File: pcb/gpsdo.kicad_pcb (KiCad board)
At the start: 2 copper layers, 120 x 100 mm, 151 parts, among them IC1 ICE40LP384-SG32, J1 JTAG, J10 CLK0, J11 CLK7, J12 USB_B_Micro, J13 CLK6, J14 CLK5, J15 CLK4, J2 SSD1306, J3 EXT_CLOCK, J4 GPS_ANT, J5 USB_B_Micro, J6 CLK3, J7 Screw_Terminal_01x03, J8 CLK2, J9 CLK1, M1 E73-2G4M08S1C-52840, Q1 S9018, SW1 EC11, SW2 MCML4-112B, U1 MCP9808_MSOP, U2 MCP9808_MSOP, U3 TPS652510, U4 LT1763xS8, U5 74LVC1G17, U6 Si5351C-B-GM, U7 74LVC1G17, U8 uBlox NEO-7M, U9 AD5761R, Y1 32768, Y2 8663-XS

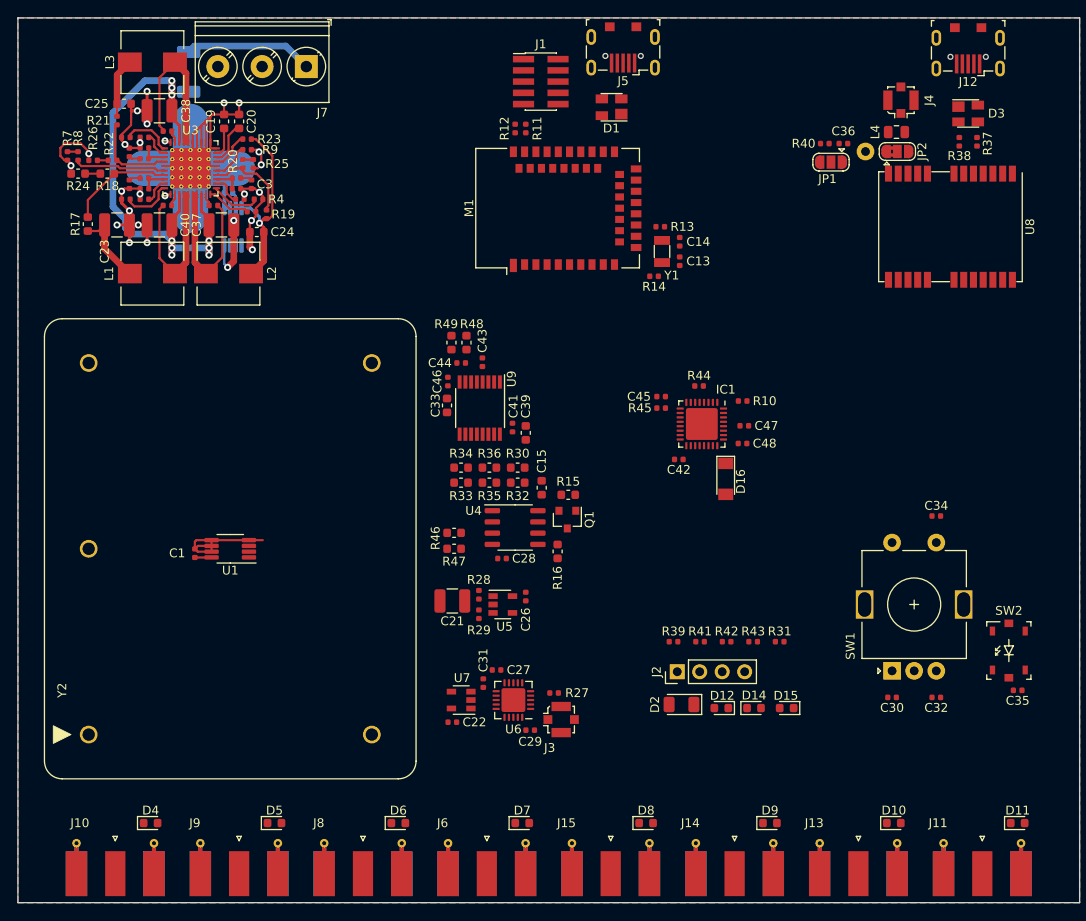
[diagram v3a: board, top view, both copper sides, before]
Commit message: pin assignment optimization, routing
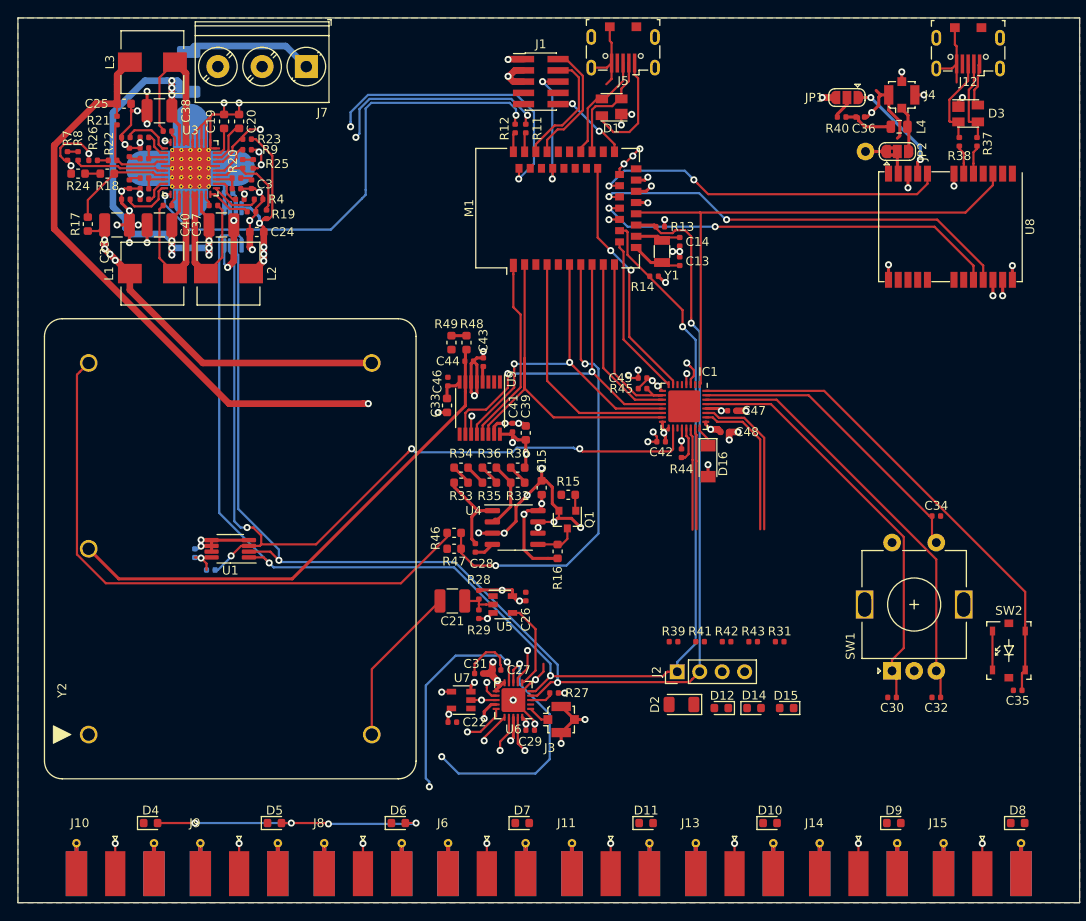
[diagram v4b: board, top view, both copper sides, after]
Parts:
- C1, R10: moved to B.Cu
- moved R10 63.1 mm to (71.8, 122.4), turned to 0 degrees
- moved D11 42.0 mm to (121.0, 151.0)
- moved D8 42.0 mm to (163.0, 151.0)
- moved J11 42.0 mm to (117.0, 155.0)
- moved J15 42.0 mm to (159.0, 155.0)
- moved D9 14.0 mm to (149.0, 151.0)
- moved J13 14.0 mm to (131.0, 155.0)
- moved J14 14.0 mm to (145.0, 155.0)
- moved D10 14.0 mm to (135.0, 151.0)
- moved R44 7.85 mm to (125.0, 109.2), turned to 270 degrees
- moved JP1 7.52 mm to (143.7, 69.0)
- moved R40 3.55 mm to (143.1, 71.2)
- moved C36 3.55 mm to (145.2, 71.2)
- moved C28 3.25 mm to (101.7, 119.9), turned to 90 degrees
- moved R45 3.04 mm to (120.6, 101.9)
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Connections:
- IC1 pad 1: (no net) -> /GPS_PULSE
- IC1 pad 18: /FPGA_INT -> /TEMP_ALERT
- IC1 pad 19: /GPS_PULSE -> (no net)
- IC1 pad 20: /ENCODER_A -> /PLL_INT_REF
- IC1 pad 22: /ENCODER_B -> /DISPLAY0
- IC1 pad 23: /ENCODER_BTN -> /DISPLAY1
- IC1 pad 26: /BTN_BLUE -> /DISPLAY2
- IC1 pad 27: /DISPLAY0 -> /BLUE_HI
- IC1 pad 29: /DISPLAY1 -> /ENCODER_A
- IC1 pad 30: /DISPLAY2 -> /ENCODER_B
- IC1 pad 31: /BLUE_HI -> /ENCODER_BTN
- IC1 pad 32: /TEMP_ALERT -> /BTN_BLUE
- IC1 pad 6: /PLL_INT_REF -> (no net)
- IC1 pad 7: (no net) -> /FPGA_INT
- M1 pad 1: /PLL_EN -> /~DAC_CS
- M1 pad 10: /~DAC_RESET -> /CRESET_B
- M1 pad 12: /~DAC_CS -> /FPGA_WDT
- M1 pad 18: /PGOOD -> /GPS_TXD
- M1 pad 2: /FAULT -> /SPI_CLK
- M1 pad 20: /EN_12V -> /GPS_RXD
- M1 pad 22: /EN_1V2 -> /~GPS_RESET
- M1 pad 28: /CDONE -> /FPGA_INT
- M1 pad 3: /OCXO_VREF -> /DAC_VAL
- M1 pad 30: /SPI_SDO -> /PLL_EN
- M1 pad 32: /SPI_SDI -> /~DAC_ALERT
- M1 pad 33: /CRESET_B -> /FAULT
- M1 pad 34: /SPI_CLK -> /~DAC_RESET
- M1 pad 35: /~FPGA_CS -> /~DAC_LOAD
- M1 pad 38: /GPS_TXD -> /PLL_INT
- M1 pad 4: /~DAC_ALERT -> /~FPGA_CS
- M1 pad 40: /GPS_RXD -> /~DAC_CLEAR
- M1 pad 42: /~GPS_RESET -> /PGOOD
- M1 pad 6: /PLL_INT -> /SPI_SDI
- M1 pad 7: /DAC_VAL -> /OCXO_VREF
- M1 pad 8: /~DAC_CLEAR -> /SPI_SDO
- M1 pad 9: /~DAC_LOAD -> /CDONE
- R11 pad 1: /FPGA_INT -> /EN_1V2
- R12 pad 1: /FPGA_WDT -> /EN_12V
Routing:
- net +12V: track 8.89 -> 201.5 mm, vias 0 -> 7
- net /SCL: track 0.00 -> 157.2 mm, vias 0 -> 3
- net /SDA: track 0.00 -> 155.4 mm, vias 0 -> 3
- net GND: track 124.5 -> 276.9 mm, vias 24 -> 69
- net +1V2: track 6.72 -> 113.0 mm, vias 0 -> 2
- net /TEMP_ALERT: track 0.00 -> 96.8 mm, vias 0 -> 4
- net Net-(R46-Pad1): track 0.00 -> 68.0 mm
- net /CLKOUT_4: track 0.00 -> 63.6 mm, vias 0 -> 2
- net /GPS_PULSE: track 0.00 -> 62.5 mm
- net Net-(C44-Pad1): track 0.00 -> 58.5 mm
- net /BTN_BLUE: track 0.00 -> 56.8 mm
- net /EN_12V: track 0.69 -> 56.2 mm, vias 1 -> 2
- net +3V3: track 25.8 -> 79.0 mm, vias 1 -> 30
- net /CLKOUT_5: track 0.00 -> 52.4 mm, vias 0 -> 2
- net /OCXO_VREF: track 0.00 -> 51.7 mm, vias 0 -> 2
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- added copper zone on In2.Cu, net +3V3
- added copper zone on In1.Cu, net GND
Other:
- copper layers 2 -> 4

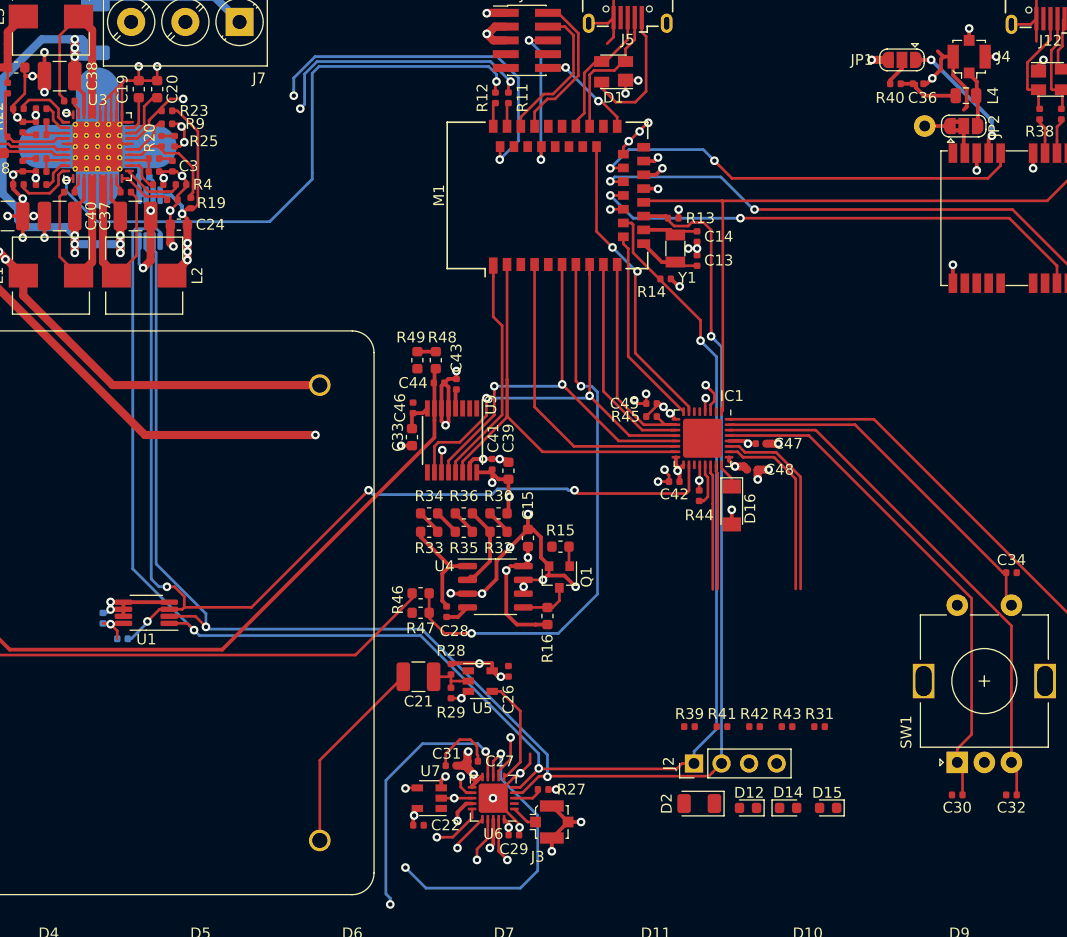
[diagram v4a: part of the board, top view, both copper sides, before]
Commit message: pin assignment optimization, routing
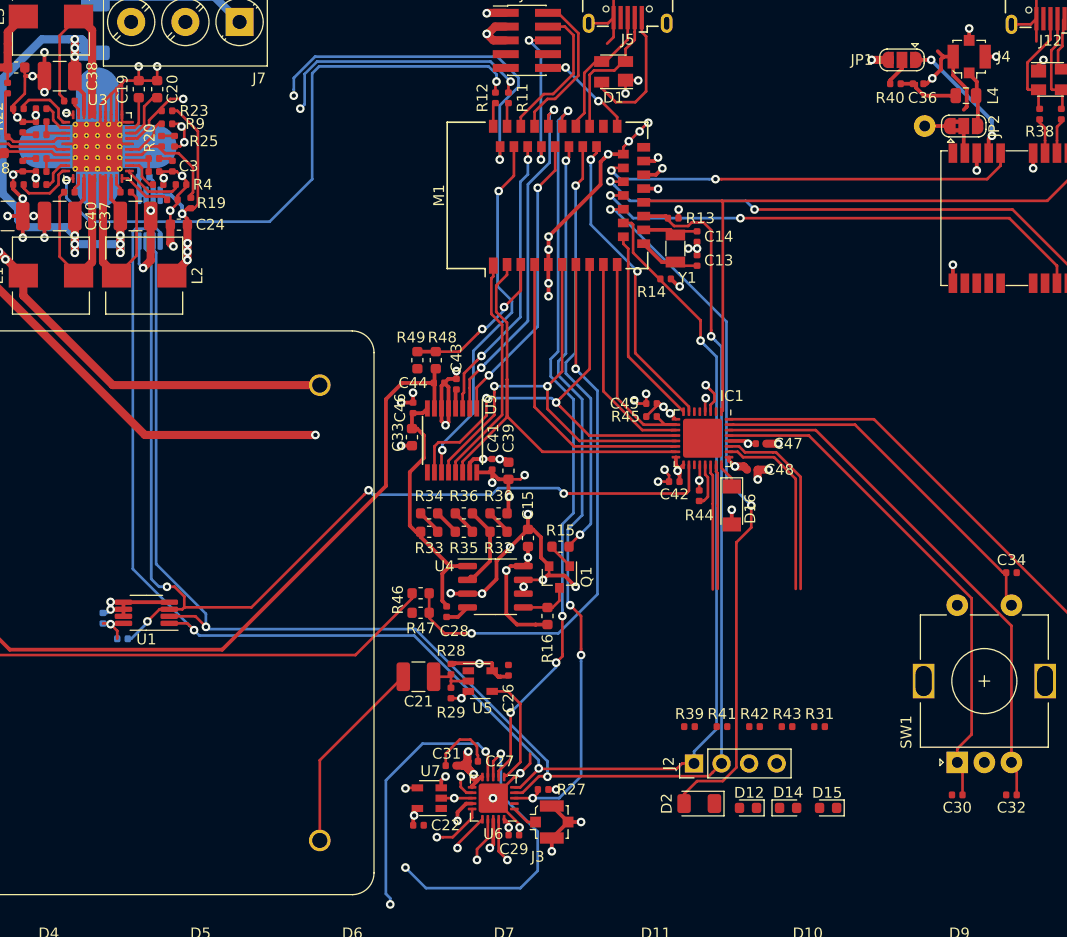
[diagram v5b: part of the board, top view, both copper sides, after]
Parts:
- moved C26 0.10 mm to (107.4, 125.3)
- turned R15 to 0 degrees
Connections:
- M1 pad 16: /~EN_10V -> /FAULT
- M1 pad 30: /PLL_EN -> /~EN_10V
- M1 pad 32: /~DAC_ALERT -> /PLL_INT
- M1 pad 33: /FAULT -> /PLL_EN
- M1 pad 34: /~DAC_RESET -> /~DAC_ALERT
- M1 pad 35: /~DAC_LOAD -> /~DAC_CLEAR
- M1 pad 38: /PLL_INT -> /~DAC_RESET
- M1 pad 40: /~DAC_CLEAR -> /~DAC_LOAD
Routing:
- net /PLL_INT: track 2.68 -> 68.4 mm, vias 0 -> 4
- net /FAULT: track 0.00 -> 65.6 mm, vias 0 -> 2
- net /PLL_EN: track 4.11 -> 67.5 mm, vias 1 -> 4
- net /~EN_10V: track 1.21 -> 39.3 mm, vias 1 -> 2
- net /~DAC_CLEAR: track 0.00 -> 32.5 mm, vias 0 -> 2
- net /~DAC_LOAD: track 2.08 -> 33.9 mm, vias 1 -> 2
- net /~DAC_ALERT: track 0.00 -> 27.1 mm, vias 0 -> 2
- net /~DAC_RESET: track 0.00 -> 26.7 mm, vias 0 -> 2
- net GND: track 276.9 -> 303.1 mm, vias 69 -> 77
- net /DAC_VAL: track 1.70 -> 14.4 mm, vias 0 -> 2
- net +10V: track 13.1 -> 24.5 mm
- net Net-(C44-Pad1): track 58.5 -> 62.5 mm
- net /SPI_SDI: track 39.7 -> 41.6 mm
- net /SPI_SDO: track 41.2 -> 42.9 mm
- net /~GPS_RESET: track 40.7 -> 39.1 mm
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
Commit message: routing progress, silkscreen
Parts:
- moved D2 61.4 mm to (124.8, 76.2)
- moved R31 53.7 mm to (124.8, 78.0), turned to 180 degrees
- moved C35 31.2 mm to (152.0, 106.8), turned to 0 degrees
- moved D11 25.1 mm to (111.0, 128.0)
- moved D4 25.1 mm to (55.0, 128.0)
- moved D5 25.1 mm to (69.0, 128.0)
- moved D6 25.1 mm to (83.0, 128.0)
- moved D7 25.1 mm to (97.0, 128.0)
- moved D8 25.1 mm to (153.0, 128.0)
- moved D9 25.1 mm to (139.0, 128.0)
- moved D10 25.1 mm to (125.0, 128.0)
- moved C30 22.4 mm to (138.8, 116.8)
- moved C32 22.4 mm to (143.8, 116.8)
- moved J3 22.4 mm to (101.4, 119.3)
- moved R27 22.4 mm to (100.6, 116.3)
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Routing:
- net /BLUE_LO: track 0.00 -> 112.4 mm, vias 0 -> 2
- net /DISPLAY1: track 11.5 -> 115.6 mm, vias 0 -> 2
- net Net-(D11-Pad1): track 0.00 -> 84.0 mm, vias 0 -> 2
- net Net-(D12-Pad1): track 0.00 -> 79.0 mm, vias 0 -> 3
- net /DISPLAY0: track 43.2 -> 108.2 mm, vias 4 -> 2
- net /BLUE_HI: track 18.1 -> 71.6 mm, vias 0 -> 2
- net /DISPLAY2: track 17.3 -> 70.1 mm, vias 0 -> 4
- net Net-(D10-Pad1): track 0.00 -> 41.3 mm
- net /FAULT: track 65.6 -> 28.6 mm
- net /CLKOUT_3: track 43.6 -> 30.3 mm, vias 3 -> 2
- net GND: track 303.1 -> 307.1 mm, vias 77 -> 219
- net Net-(D2-Pad1): track 0.00 -> 2.13 mm
- net +1V2: track 113.0 -> 111.1 mm
- net /CLKOUT_2: track 38.5 -> 37.7 mm
- net /SCL: track 156.8 -> 157.5 mm
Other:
- board text added: "14-16V, 1A GND GND"
- board text added: "GND, GND, 14-16V, 1A"
- board text added: "OUT0"
- board text added: "OUT1"
- board text added: "OUT2"
- board text added: "OUT3"
- board text added: "OUT4"
- board text added: "OUT5"
- board text added: "OUT6"
- board text added: "OUT7"
- board text added: "fault"

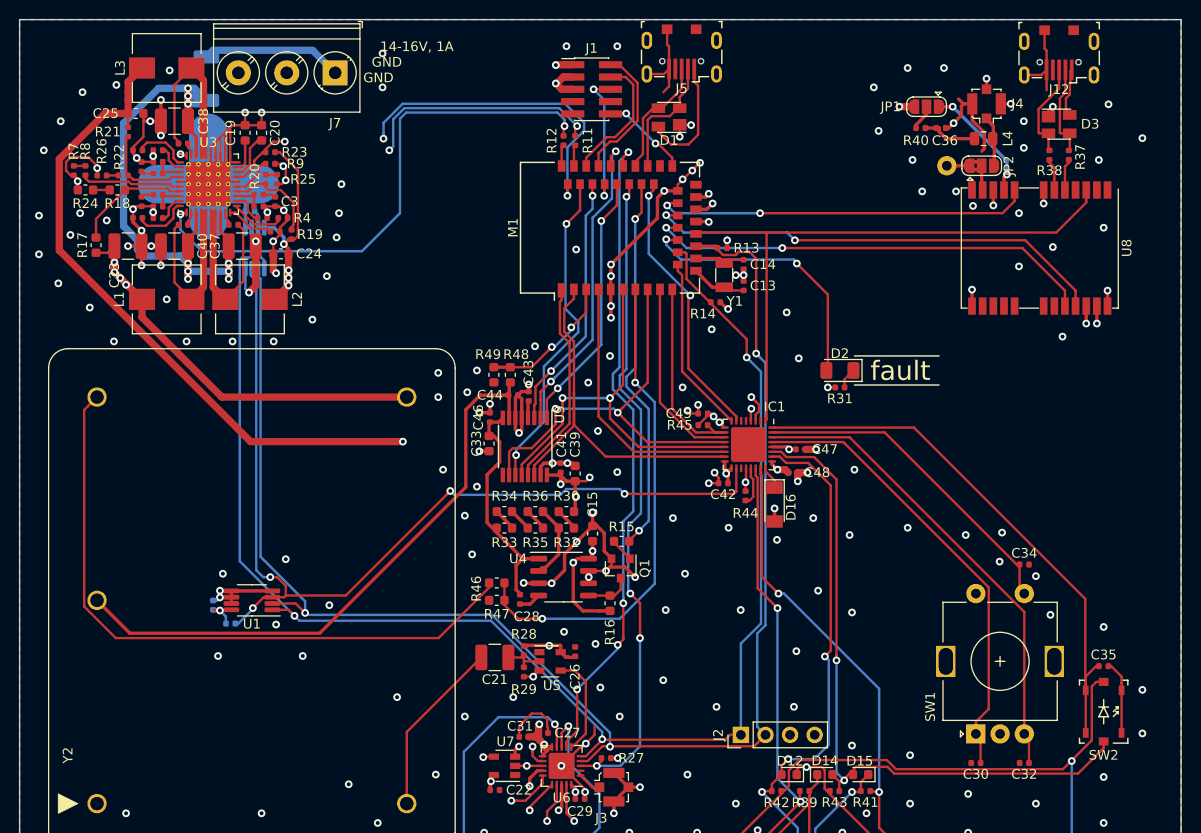
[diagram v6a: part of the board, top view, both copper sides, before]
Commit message: more layout cleanup
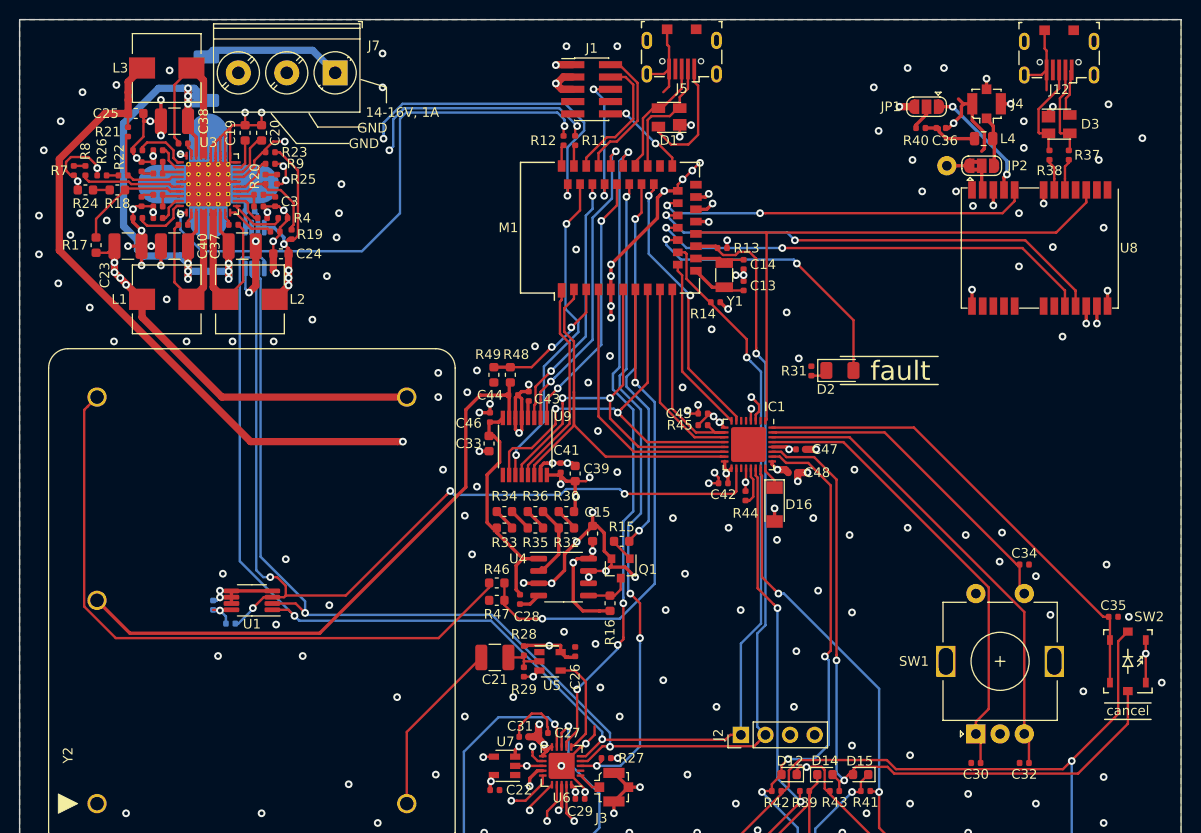
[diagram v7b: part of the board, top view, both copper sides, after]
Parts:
- moved SW2 5.77 mm to (154.5, 106.3)
- moved C35 5.20 mm to (153.0, 101.7)
- moved R31 3.40 mm to (121.8, 76.3), turned to 90 degrees
- turned D2 to 0 degrees
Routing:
- net /BTN_BLUE: track 56.8 -> 49.7 mm
- net /BLUE_HI: track 71.6 -> 77.8 mm
- net /BLUE_LO: track 112.4 -> 118.2 mm
- net GND: track 307.1 -> 303.1 mm, vias 219 -> 220
- net /FAULT: track 28.6 -> 29.6 mm
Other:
- board text added: "GND /GND /14-16V 1A"
- board text added: "cancel"
- board text removed: "GND, GND, 14-16V, 1A"
